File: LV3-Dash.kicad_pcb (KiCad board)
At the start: 2 copper layers, 90 x 50 mm, 93 parts, among them J1 USB_C_Receptacle_USB2.0_16P, J2 FTSH-105-01-L-DV-K-A, J3 Conn_01x04_MountingPin, J4 Conn_01x05_Pin, J5 Conn_01x05_MountingPin, J6 MSD-11-A, J7 62684-401100AHLF, U1 STM32H743VITx, U2 TJA1051T-3, U4 LMR51625YDDCR, U5 TLV74033PDBVR, U6 AP3032KTR, U7 AMS1117-3.3, Y1 Crystal_GND24

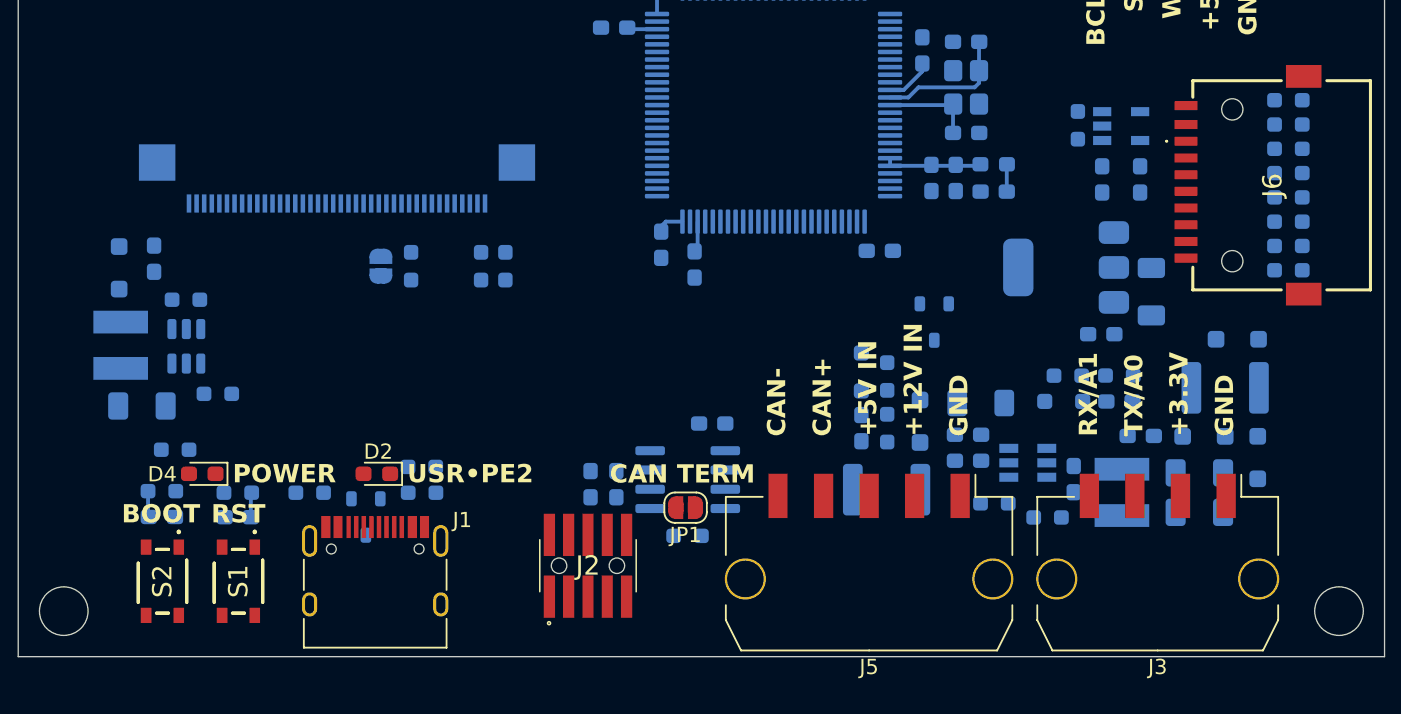
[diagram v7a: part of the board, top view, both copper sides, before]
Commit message: some preliminary routing
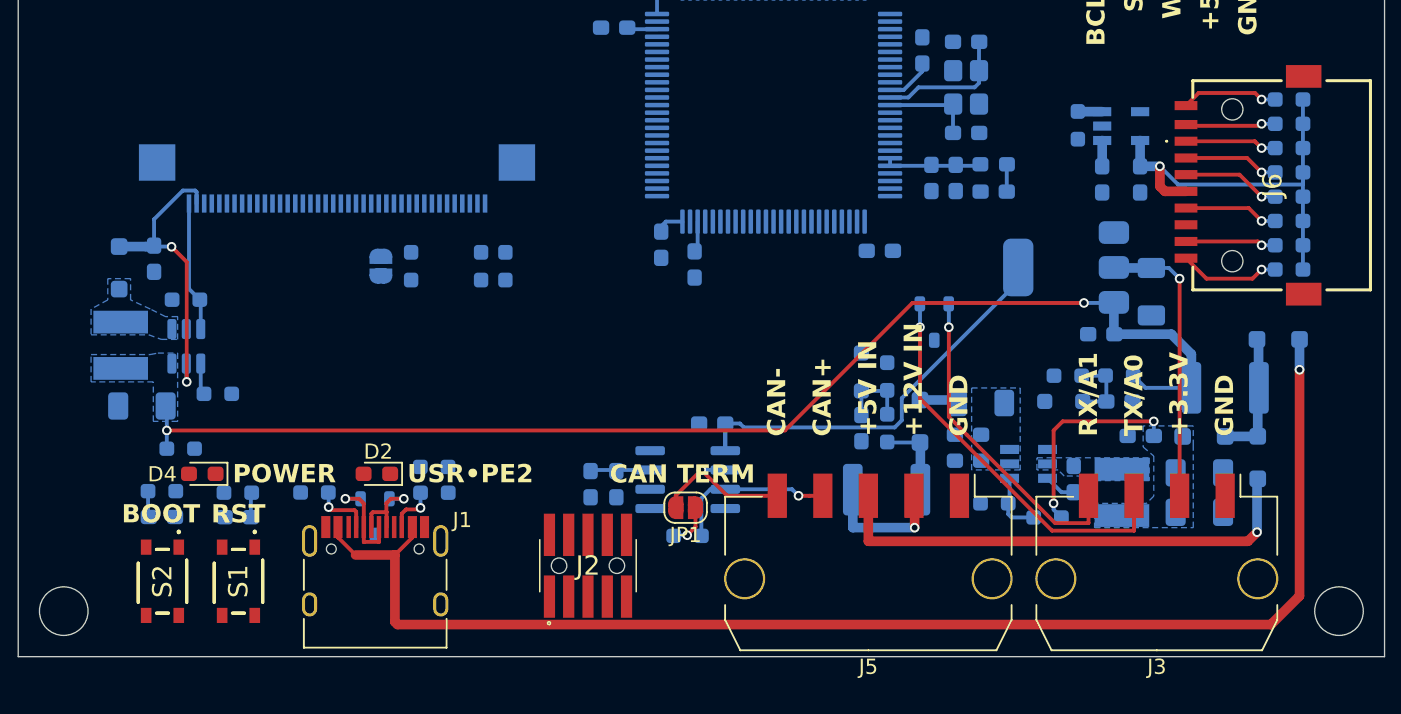
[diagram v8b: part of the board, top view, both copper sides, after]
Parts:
- moved D7 2.70 mm to (133.0, 79.1), turned to 0 degrees
- moved R4 0.81 mm to (77.4, 89.2)
- moved R5 0.81 mm to (77.4, 87.5)
- moved D1 0.60 mm to (73.5, 90.8)
- moved R17 0.37 mm to (60.7, 86.3)
- moved R3 0.31 mm to (69.5, 89.2)
- moved U4 0.09 mm to (116.5, 87.3)
- moved R9 0.06 mm to (133.7, 71.3)
- moved R10 0.06 mm to (133.7, 69.7)
- moved R11 0.06 mm to (133.7, 68.1)
- moved R12 0.06 mm to (133.7, 66.5)
- moved R13 0.06 mm to (133.7, 64.9)
- moved R14 0.06 mm to (133.7, 63.3)
- moved R7 0.06 mm to (133.7, 74.5)
- moved R8 0.06 mm to (133.7, 72.9)
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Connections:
- D11 pad 1: DPAD_A1 -> DPAD_A0
- D11 pad 2: DPAD_A0 -> DPAD_A1
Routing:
- net +5V_USB: track 0.00 -> 89.0 mm, vias 0 -> 1
- net +5V: track 0.00 -> 88.7 mm, vias 0 -> 2
- net +3.3V: track 10.7 -> 58.1 mm, vias 0 -> 1
- net +5V_BUS: track 0.00 -> 32.4 mm, vias 0 -> 1
- net +3.3V_SD: track 0.00 -> 28.1 mm, vias 0 -> 1
- net DPAD_A0: track 0.00 -> 26.2 mm, vias 0 -> 1
- net DPAD_A1: track 0.00 -> 21.3 mm, vias 0 -> 1
- net BKLT+: track 0.00 -> 20.7 mm, vias 0 -> 2
- net +5V_BUCK: track 0.00 -> 13.8 mm, vias 0 -> 2
- net PRIMARY_CAN+: track 0.00 -> 10.9 mm, vias 0 -> 1
- net PRIMARY_CAN-: track 0.00 -> 10.5 mm, vias 0 -> 1
- net +12V_IN: track 0.00 -> 8.66 mm, vias 0 -> 1
- net BKLT-: track 0.00 -> 8.59 mm
- net Net-(D6-K): track 0.00 -> 8.58 mm
- net USB-: track 0.00 -> 6.85 mm, vias 0 -> 1
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- added copper zone on B.Cu, net +5V
- added copper zone on B.Cu, net +5V_BUCK
- added copper zone on B.Cu, net Net-(D10-A)
- added copper zone on B.Cu, net Net-(U4-EN)
- added copper zone on B.Cu, net Net-(U4-SW)
